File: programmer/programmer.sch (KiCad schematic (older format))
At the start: 18 parts

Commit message: Added first revision of programmer board
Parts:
- removed C? (x2): 47pF, symbol Device:C
- C3, C4, C5: renamed from C?; footprint (none) -> Capacitor_SMD:C_0603_1608Metric
- D1, D2: renamed from D?; footprint (none) -> Capacitor_SMD:C_0603_1608Metric
- J1: renamed from J?; footprint (none) -> digikey-footprints:USB_Micro_B_Female_10118192
- J2: renamed from J?; footprint (none) -> Connector_PinSocket_2.54mm:PinSocket_2x05_P2.54mm_Vertical
- Q1: renamed from Q?; footprint (none) -> digikey-footprints:SOT-23-3
- R1, R2: renamed from R?; value R -> 27; footprint (none) -> Capacitor_SMD:C_0603_1608Metric
- R3, R4, R5: renamed from R?; footprint (none) -> Capacitor_SMD:C_0603_1608Metric
- SW1, SW2: renamed from SW?; footprint (none) -> My Footprints:222CMVBAR
- U1: renamed from U?; footprint digikey-footprints:SOIC-16_W3.90mm -> Package_SO:SSOP-16_3.9x4.9mm_P0.635mm
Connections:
- no-connect marks 3 -> 9
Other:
- moved on the sheet: R1, R2

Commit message: Changed programmer parts to LCSC parts, added part numbers
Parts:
- removed SW1, SW2: 222CMVBAR, My Footprints:222CMVBAR, symbol My_Symbols:222CMVBAR
- added SW1, SW2: SW_SPST, Button_Switch_SMD:SW_Push_1P1T_NO_6x6mm_H9.5mm, symbol Switch:SW_SPST
- C3: LCSC Part Number (none) -> C99226
- C4, C5: LCSC Part Number (none) -> C24452
- J1: LCSC Part Number (none) -> C132564
- Q1: LCSC Part Number (none) -> C71533
- R1, R2: LCSC Part Number (none) -> C137639
- R3: LCSC Part Number (none) -> C99198
- R4, R5: LCSC Part Number (none) -> C137641
- RX1: renamed from D1; LCSC Part Number (none) -> C125094
- TX1: renamed from D2; LCSC Part Number (none) -> C99290
- U1: LCSC Part Number (none) -> C69082
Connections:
- wire segments 74 -> 64
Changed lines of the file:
@@
 EESchema Schematic File Version 4
-LIBS:programmer-cache
 EELAYER 30 0
 EELAYER END
@@
 $EndDescr
 $Comp
-L My_Symbols:222CMVBAR SW1
-U 1 1 5DF12375
-P 3100 5250
-F 0 "SW1" V 3146 5156 50  0000 R CNN
-F 1 "222CMVBAR" V 3055 5156 50  0000 R CNN
-F 2 "My Footprints:222CMVBAR" H 3100 5450 50  0001 C CNN
-F 3 "~" H 3100 5450 50  0001 C CNN
-	1    3100 5250
-	0    -1   -1   0
-$EndComp
-$Comp
-L My_Symbols:222CMVBAR SW2
-U 1 1 5DF13400
-P 5500 5250
-F 0 "SW2" V 5546 5156 50  0000 R CNN
-F 1 "222CMVBAR" V 5455 5156 50  0000 R CNN
-F 2 "My Footprints:222CMVBAR" H 5500 5450 50  0001 C CNN
-F 3 "~" H 5500 5450 50  0001 C CNN
-	1    5500 5250
-	0    -1   -1   0
-$EndComp
-$Comp
 L My_Symbols:10118192-0001LF J1
 U 1 1 5DF14664
@@
 F 2 "digikey-footprints:USB_Micro_B_Female_10118192" H 3200 1900 50  0001 C CNN
 F 3 "~" H 3200 1900 50  0001 C CNN
+F 4 "C132564" H 3050 1950 50  0001 C CNN "LCSC Part Number"
 	1    3050 1950
 	1    0    0    -1
@@
 F 11 "FTDI, Future Technology Devices International Ltd" H 7600 5950 60  0001 L CNN "Manufacturer"
 F 12 "Active" H 7600 6050 60  0001 L CNN "Status"
+F 13 "C69082" H 7400 4850 50  0001 C CNN "LCSC Part Number"
 	1    7400 4850
 	1    0    0    -1
@@
 F 2 "Capacitor_SMD:C_0603_1608Metric" V 3680 1950 50  0001 C CNN
 F 3 "~" H 3750 1950 50  0001 C CNN
+F 4 " C137639" H 3750 1950 50  0001 C CNN "LCSC Part Number"
 	1    3750 1950
 	0    1    1    0
@@
 F 2 "Capacitor_SMD:C_0603_1608Metric" V 3680 2050 50  0001 C CNN
 F 3 "~" H 3750 2050 50  0001 C CNN
+F 4 " C137639" H 3750 2050 50  0001 C CNN "LCSC Part Number"
 	1    3750 2050
 	0    1    1    0
@@
 F 2 "Capacitor_SMD:C_0603_1608Metric" H 6638 1900 50  0001 C CNN
 F 3 "~" H 6600 2050 50  0001 C CNN
+F 4 " C99226" H 6600 2050 50  0001 C CNN "LCSC Part Number"
+F 5 "" H 6600 2050 50  0001 C CNN "Tolerance"
 	1    6600 2050
 	1    0    0    -1
@@
 F 2 "Capacitor_SMD:C_0603_1608Metric" H 7088 1900 50  0001 C CNN
 F 3 "~" H 7050 2050 50  0001 C CNN
+F 4 "C24452" H 7050 2050 50  0001 C CNN "LCSC Part Number"
+F 5 "" H 7050 2050 50  0001 C CNN "Tolerance"
 	1    7050 2050
 	1    0    0    -1
@@
 RX
 $Comp
-L Device:LED D2
+L Device:LED TX1
 U 1 1 5DF27966
 P 8850 4850
-F 0 "D2" V 8889 4733 50  0000 R CNN
+F 0 "TX1" V 8889 4733 50  0000 R CNN
 F 1 "LED" V 8798 4733 50  0000 R CNN
 F 2 "Capacitor_SMD:C_0603_1608Metric" H 8850 4850 50  0001 C CNN
 F 3 "~" H 8850 4850 50  0001 C CNN
+F 4 "C99290" H 8850 4850 50  0001 C CNN "LCSC Part Number"
 	1    8850 4850
 	0    -1   -1   0
 $EndComp
 $Comp
-L Device:LED D1
+L Device:LED RX1
 U 1 1 5DF26D46
 P 8500 4850
-F 0 "D1" V 8539 4733 50  0000 R CNN
+F 0 "RX1" V 8539 4733 50  0000 R CNN
 F 1 "LED" V 8448 4733 50  0000 R CNN
 F 2 "Capacitor_SMD:C_0603_1608Metric" H 8500 4850 50  0001 C CNN
 F 3 "~" H 8500 4850 50  0001 C CNN
+F 4 "C125094 " H 8500 4850 50  0001 C CNN "LCSC Part Number"
 	1    8500 4850
 	0    -1   -1   0
@@
 F 2 "Capacitor_SMD:C_0603_1608Metric" V 8430 4500 50  0001 C CNN
 F 3 "~" H 8500 4500 50  0001 C CNN
+F 4 "C137641" H 8500 4500 50  0001 C CNN "LCSC Part Number"
 	1    8500 4500
 	1    0    0    -1
@@
 F 2 "Capacitor_SMD:C_0603_1608Metric" V 8780 4500 50  0001 C CNN
 F 3 "~" H 8850 4500 50  0001 C CNN
+F 4 "C137641" H 8850 4500 50  0001 C CNN "LCSC Part Number"
 	1    8850 4500
 	1    0    0    -1
@@
 F 2 "Capacitor_SMD:C_0603_1608Metric" V 3030 4650 50  0001 C CNN
 F 3 "~" H 3100 4650 50  0001 C CNN
+F 4 "C99198" H 3100 4650 50  0001 C CNN "LCSC Part Number"
 	1    3100 4650
 	1    0    0    -1
@@
 	3100 4500 3100 4300
 Wire Wire Line
-	3100 5450 3100 5550
-Wire Wire Line
-	5500 5650 5500 5550
-Wire Wire Line
 	5500 5050 5500 4950
-Wire Wire Line
-	5550 5050 5550 4950
-Wire Wire Line
-	5550 4950 5500 4950
-Wire Wire Line
-	5550 5450 5550 5550
-Wire Wire Line
-	5550 5550 5500 5550
-Connection ~ 5500 5550
-Wire Wire Line
-	5500 5550 5500 5450
-Wire Wire Line
-	3150 5450 3150 5550
-Wire Wire Line
-	3150 5550 3100 5550
-Connection ~ 3100 5550
-Wire Wire Line
-	3100 5550 3100 5650
-Wire Wire Line
-	3150 5050 3150 4950
-Wire Wire Line
-	3150 4950 3100 4950
 Connection ~ 3100 4950
 Wire Wire Line
@@
 Text GLabel 3400 4950 2    50   Input ~ 0
 BOOT
-Wire Wire Line
-	3150 4950 3400 4950
 Text GLabel 5750 4950 2    50   Input ~ 0
 EN
@@
 F 2 "digikey-footprints:SOT-23-3" H 5200 4950 50  0001 C CNN
 F 3 "~" H 5000 4850 50  0001 C CNN
+F 4 " C71533" H 5000 4850 50  0001 C CNN "LCSC Part Number"
 	1    5000 4850
 	0    1    1    0
@@
 	5200 4950 5500 4950
 Connection ~ 5500 4950
-Wire Wire Line
-	5550 4950 5750 4950
-Connection ~ 5550 4950
-Connection ~ 3150 4950
 Wire Wire Line
 	4700 4950 4800 4950
@@
 F 2 "Capacitor_SMD:C_0603_1608Metric" H 8088 5200 50  0001 C CNN
 F 3 "~" H 8050 5350 50  0001 C CNN
+F 4 "C24452" H 8050 5350 50  0001 C CNN "LCSC Part Number"
+F 5 "" H 8050 5350 50  0001 C CNN "Tolerance"
 	1    8050 5350
 	1    0    0    -1
@@
 Wire Wire Line
 	3350 2050 3600 2050
+$Comp
+L Switch:SW_SPST SW1
+U 1 1 5DF6048C
+P 3100 5250
+F 0 "SW1" V 3146 5162 50  0000 R CNN
+F 1 "SW_SPST" V 3055 5162 50  0000 R CNN
+F 2 "Button_Switch_SMD:SW_Push_1P1T_NO_6x6mm_H9.5mm" H 3100 5250 50  0001 C CNN
+F 3 "~" H 3100 5250 50  0001 C CNN
+F 4 "C221880" H 3100 5250 50  0001 C CNN "LCSC Part Number"
+	1    3100 5250
+	0    -1   -1   0
+$EndComp
+$Comp
+L Switch:SW_SPST SW2
+U 1 1 5DF60D14
+P 5500 5250
+F 0 "SW2" V 5546 5162 50  0000 R CNN
+F 1 "SW_SPST" V 5455 5162 50  0000 R CNN
+F 2 "Button_Switch_SMD:SW_Push_1P1T_NO_6x6mm_H9.5mm" H 5500 5250 50  0001 C CNN
+F 3 "~" H 5500 5250 50  0001 C CNN
+F 4 "C221880" H 5500 5250 50  0001 C CNN "LCSC Part Number"
+	1    5500 5250
+	0    -1   -1   0
+$EndComp
+Wire Wire Line
+	5500 4950 5750 4950
+Wire Wire Line
+	5500 5450 5500 5650
+Wire Wire Line
+	3100 5450 3100 5650
+Wire Wire Line
+	3100 4950 3400 4950
 $EndSCHEMATC

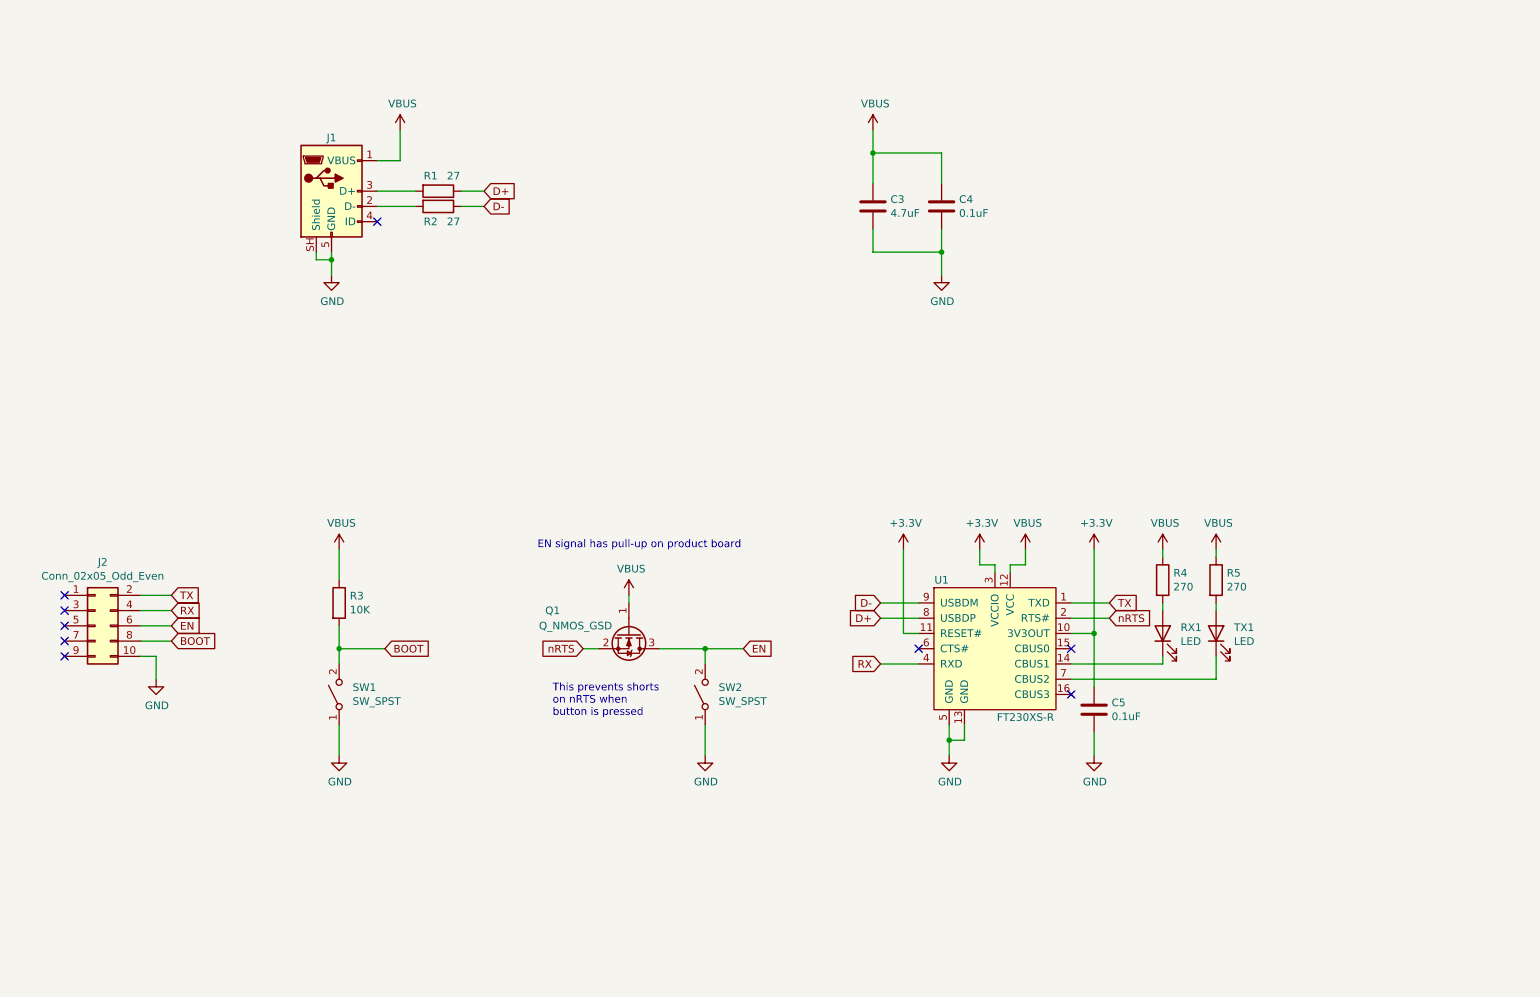
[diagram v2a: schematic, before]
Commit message: Added .gitignore and added BOMs for programmer
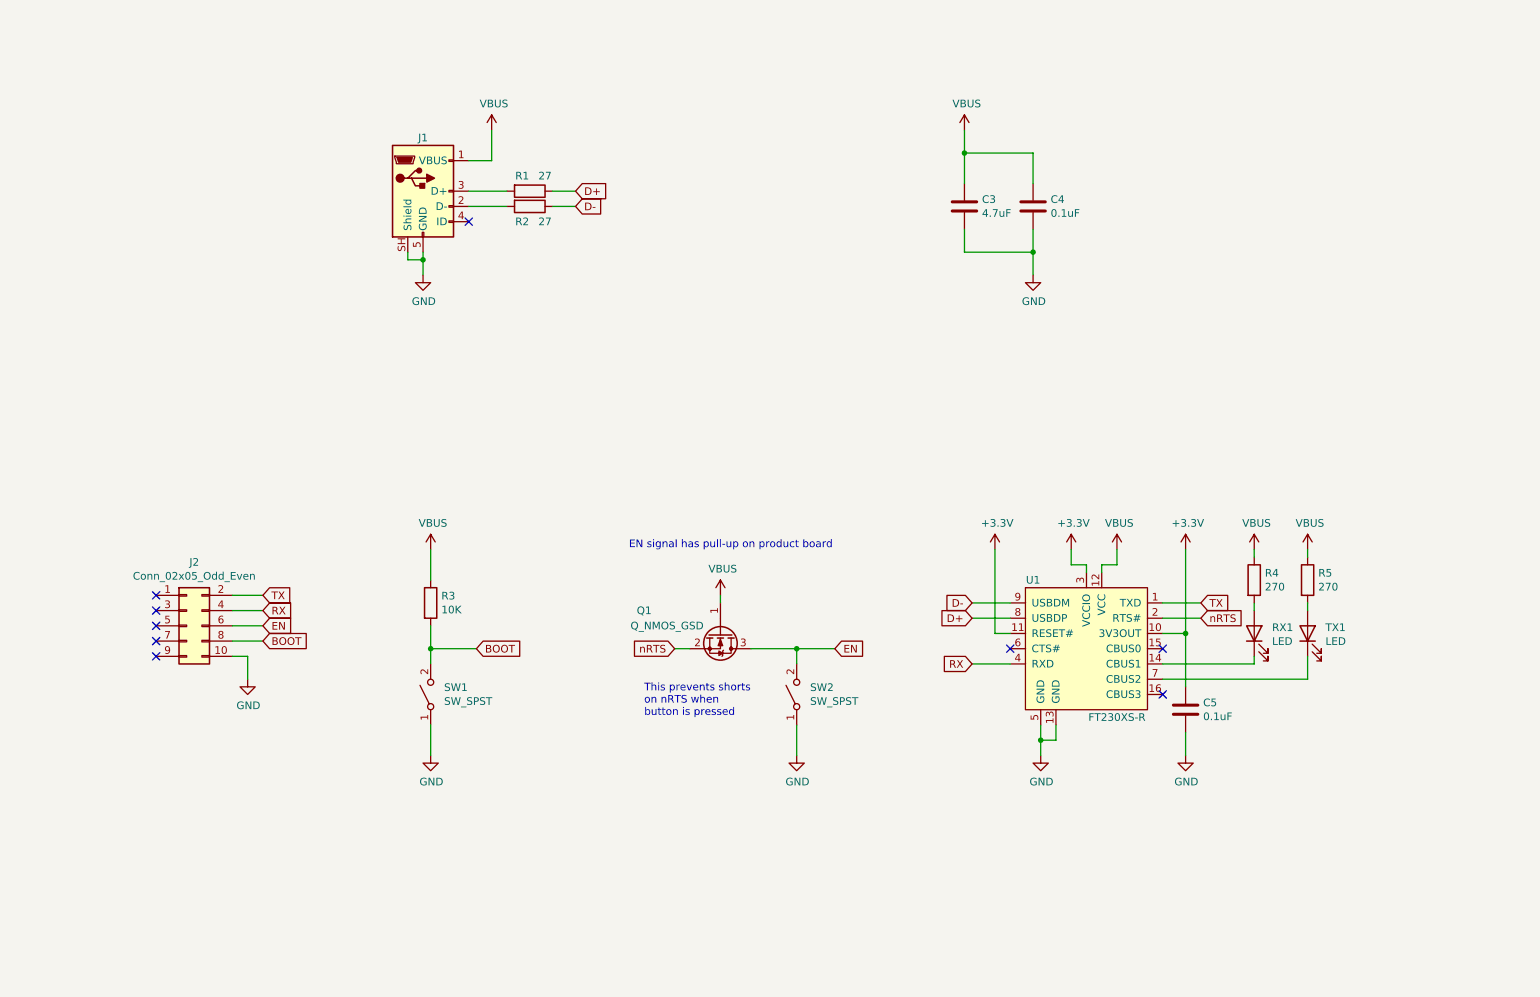
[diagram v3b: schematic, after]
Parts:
- J2: LCSC Part Number (none) -> Unpopulated
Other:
- moved on the sheet: C3, C4, C5, J1, J2, Q1, R1, R2, R3, R4, R5, RX1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

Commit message: Updated programmer to include jtag and dtr signals. Swapped FT230X for FT2232HL
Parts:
- removed C4: 0.1uF, Capacitor_SMD:C_0603_1608Metric, symbol Device:C
- removed R5: 270, Capacitor_SMD:C_0603_1608Metric, symbol Device:R
- removed RX1, TX1: LED, Capacitor_SMD:C_0603_1608Metric, symbol Device:LED
- removed SW1, SW2: SW_SPST, Button_Switch_SMD:SW_Push_1P1T_NO_6x6mm_H9.5mm, symbol Switch:SW_SPST
- removed U1: FT230XS-R, Package_SO:SSOP-16_3.9x4.9mm_P0.635mm, symbol dk_Interface-Controllers:FT230XS-R
- added C1, C2, C6, C7, C8, C9: 0.1uF, Capacitor_SMD:C_0603_1608Metric, symbol Device:C
- added D1: BLU, LED_SMD:LED_0603_1608Metric, symbol Device:LED
- added D2: GRN, LED_SMD:LED_0603_1608Metric, symbol Device:LED
- added Q?: 2N7002ET1G, Package_TO_SOT_SMD:SOT-23, symbol Device:Q_NMOS_GSD
- added U1: TLV75533PDBV, Package_TO_SOT_SMD:SOT-23-5, symbol Regulator_Linear:TLV75533PDBV
- added U2: FT2232HL, Package_QFP:LQFP-64_10x10mm_P0.5mm, symbol Interface_USB:FT2232HL
- added U3: ASDMB-12.000MHz, Oscillator:Oscillator_SMD_Abracon_ASDMB-4Pin_2.5x2.0mm, symbol Oscillator:ASDMB-xxxMHz
- C3: value 4.7uF -> 1uF; LCSC Part Number C99226 -> (none); Rating (none) -> 10V
- C5: LCSC Part Number C24452 -> (none); Rating (none) -> 10V
- J1: footprint digikey-footprints:USB_Micro_B_Female_10118192 -> Esper_Footprints:AMPHENOL_10118192-0001LF; symbol My_Symbols:10118192-0001LF -> programmer-rescue:10118192-0001LF-My_Symbols; Digikey Part Number (none) -> 1175-1627-ND; LCSC Part Number C132564 -> (none)
- J2: value Conn_02x05_Odd_Even -> 3220-10-0100-00; footprint Connector_PinSocket_2.54mm:PinSocket_2x05_P2.54mm_Vertical -> Esper_Footprints:CNC_3220-10-0100-00; Digikey Part Number (none) -> 1175-1627-ND; LCSC Part Number Unpopulated -> (none)
- Q1: value Q_NMOS_GSD -> 2N7002ET1G; footprint digikey-footprints:SOT-23-3 -> Package_TO_SOT_SMD:SOT-23; Digikey Part Number (none) -> 2N7002ET1GOSCT-ND; LCSC Part Number C71533 -> (none)
- R1, R2: value 27 -> 12K; footprint Capacitor_SMD:C_0603_1608Metric -> Resistor_SMD:R_0603_1608Metric; LCSC Part Number C137639 -> (none)
- R3: value 10K -> 470; footprint Capacitor_SMD:C_0603_1608Metric -> Resistor_SMD:R_0603_1608Metric; LCSC Part Number C99198 -> (none); Rating (none) -> 1/10W
- R4: value 270 -> 470; footprint Capacitor_SMD:C_0603_1608Metric -> Resistor_SMD:R_0603_1608Metric; LCSC Part Number C137641 -> (none); Rating (none) -> 1/10W
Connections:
- net +3V3: now also R2.2, C2.1, C6.1, C7.1, C8.1, C9.1, U1.5 (OUT), U2.20 (VCCIO), U2.31 (VCCIO), U2.4 (VPHY), U2.42 (VCCIO), U2.50 (VREGIN), U2.56 (VCCIO), U2.9 (VPLL), U3.1 (Standby), U3.4 (VDD); no longer C5.1
- net D+: now also J1.3 (D+), U2.8 (DP); no longer R1.1
- net D-: now also J1.2 (D-), U2.7 (DM); no longer R2.1
- net GND: now also R1.2, C1.2, C2.2, C6.2, C7.2, C8.2, C9.2, U1.2 (GND), U2.1 (GND), U2.10 (AGND), U2.11 (GND), U2.13 (TEST), U2.15 (GND), U2.25 (GND), U2.35 (GND), U2.47 (GND), U2.5 (GND), U2.51 (GND), U3.2 (GND)
- net RX: now also U2.17 (ADBUS1)
- net TX: now also U2.16 (ADBUS0)
- net VBUS: now also C1.1, D1.2 (A), D2.2 (A), U1.1 (IN), U1.3 (EN); no longer C3.1, Q1.1 (G), R3.1, R4.1
- net TMS: now reaches J2.1 (Pin_1)
- net TMS: now also U2.41 (BDBUS3)
- net TDI: now reaches J2.3 (Pin_3)
- net TDI: now also U2.39 (BDBUS1)
- net TCK: now reaches J2.5 (Pin_5)
- net TCK: now also U2.38 (BDBUS0)
- net TDO: now reaches J2.7 (Pin_7)
- net TDO: now also U2.40 (BDBUS2)
- net RXLED#: now reaches R4.2
- net RXLED#: now also U2.29 (ACBUS3)
- net BOOT renamed IO0
- net IO0: now also Q?.3 (D); no longer R3.2
- net nRTS renamed RTS#
- net RTS#: now also Q?.1 (G), U2.18 (ADBUS2)
- new net: D1.1 (K), R3.1
- new net: D2.1 (K), R4.1
- new net +1V8: C3.1, C5.1, U2.12 (VCORE), U2.37 (VCORE), U2.49 (VREGOUT), U2.64 (VCORE)
- new net DTR#: Q1.1 (G), Q?.2 (S), U2.21 (ADBUS4)
- new net OSCI: U2.2 (OSCI), U3.3 (Out)
- new net REF: R1.1, U2.6 (REF)
- new net RESET: R2.1, U2.14 (~RESET)
- new net TXLED#: R3.2, U2.30 (ACBUS4)
- no-connect marks 9 -> 30
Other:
- note removed: "EN signal has pull-up on product board"
- note removed: "This prevents shorts\non nRTS when\nbutton is pressed"
- moved on the sheet: J1, J2
